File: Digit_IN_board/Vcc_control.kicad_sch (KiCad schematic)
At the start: 21 parts, among them Q10 DTC114ECA (SOT-23), Q4 Si2309CDS (SOT-23), Q5 DTC114ECA (SOT-23), Q7 DTC114ECA (SOT-23), Q8 DTC114ECA (SOT-23)

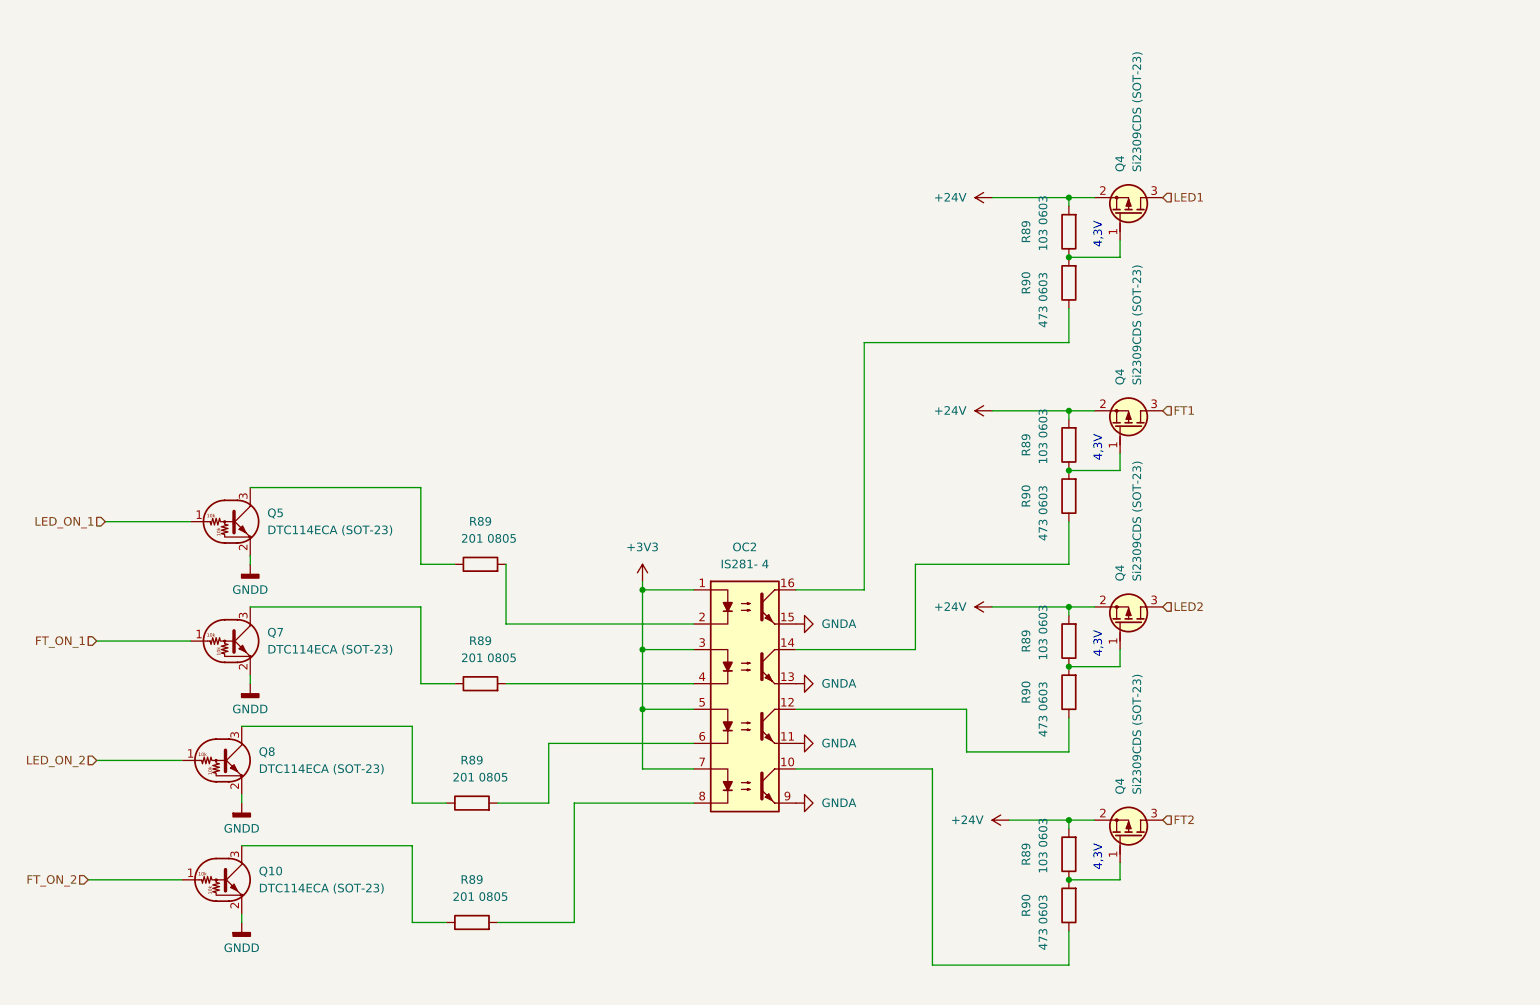
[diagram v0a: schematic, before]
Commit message: Modify Digit_IN, Motherbord, Step motors
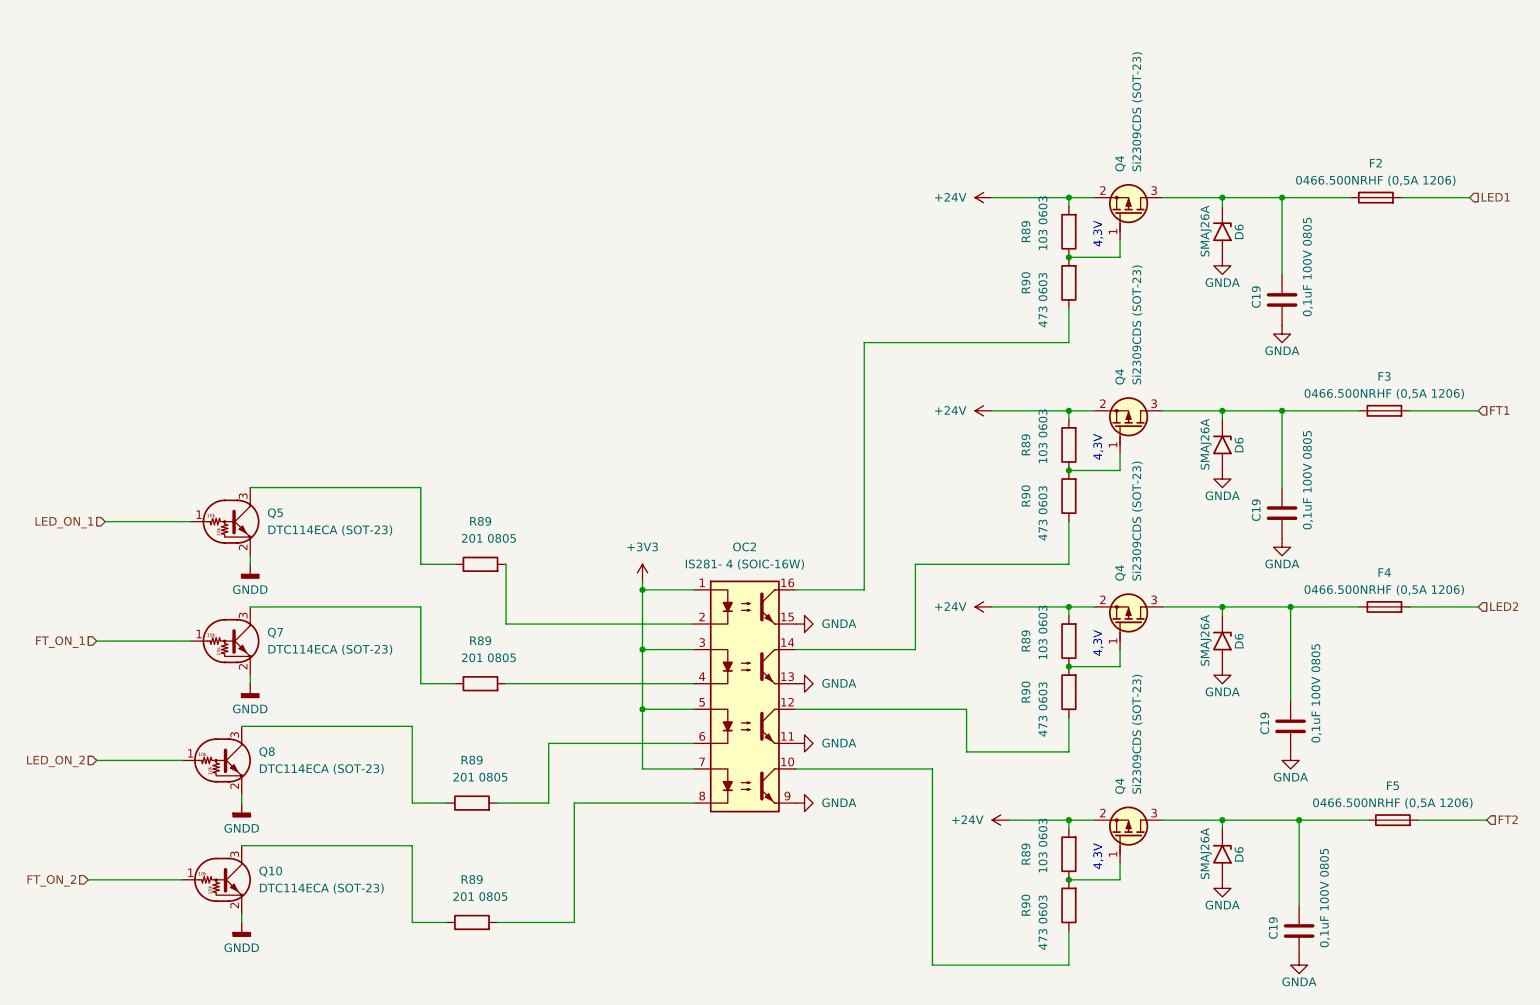
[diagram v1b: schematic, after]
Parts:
- added C19 (x4): 0,1uF 100V 0805, PCM_Resistor_SMD_AKL:R_0805_2012Metric_Pad1.20x1.40mm_HandSolder, symbol Device:C
- added D6 (x4): SMAJ26A, Diode_SMD:D_SMA, symbol Diode:SMAJ26A
- added F2, F3, F4, F5: 0466.500NRHF (0,5А 1206), PCM_Resistor_SMD_AKL:R_1206_3216Metric_Pad1.42x1.75mm_HandSolder, symbol Device:Fuse
- OC2: value IS281- 4 -> IS281- 4 (SOIC-16W)
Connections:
- net FT1: now also F3.2; no longer Q4.3 (D)
- net FT2: now also F5.2; no longer Q4.3 (D)
- net GNDA: now also C19.2, C19.2, C19.2, C19.2, D6.2 (A2), D6.2 (A2), D6.2 (A2), D6.2 (A2)
- net LED1: now also F2.2; no longer Q4.3 (D)
- net LED2: now also F4.2; no longer Q4.3 (D)
- new net: C19.1, D6.1 (A1), F4.1, Q4.3 (D)
- new net: C19.1, D6.1 (A1), F3.1, Q4.3 (D)
- new net: C19.1, D6.1 (A1), F2.1, Q4.3 (D)
- new net: C19.1, D6.1 (A1), F5.1, Q4.3 (D)
